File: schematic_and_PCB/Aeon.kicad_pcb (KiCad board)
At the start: 2 copper layers, 70 x 52 mm, 137 parts, among them IC1 AEM10941-QFN, IC2 STM32L412K8T6, IC3 FM25L04B-GTR, IC4 TPS7A0233PDBVR, J1 Conn_01x06_Pin, J2 FH34SRJ-50S-0.5SH50 - Colour 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, J3 Micro_SD_Card, Q1 BSS138, Q2 SI2301CDS-T1-E3, Q4 SI2301CDS-T1-E3, Q5 BSS138, SW1 SW_EHV_EN, SW2 REFRESH_BTN, SW3 RESET_BTN, SW4 SW_DIP_x06_SMD_1.27, SW5 SW_DIP_x06_SMD_1.27

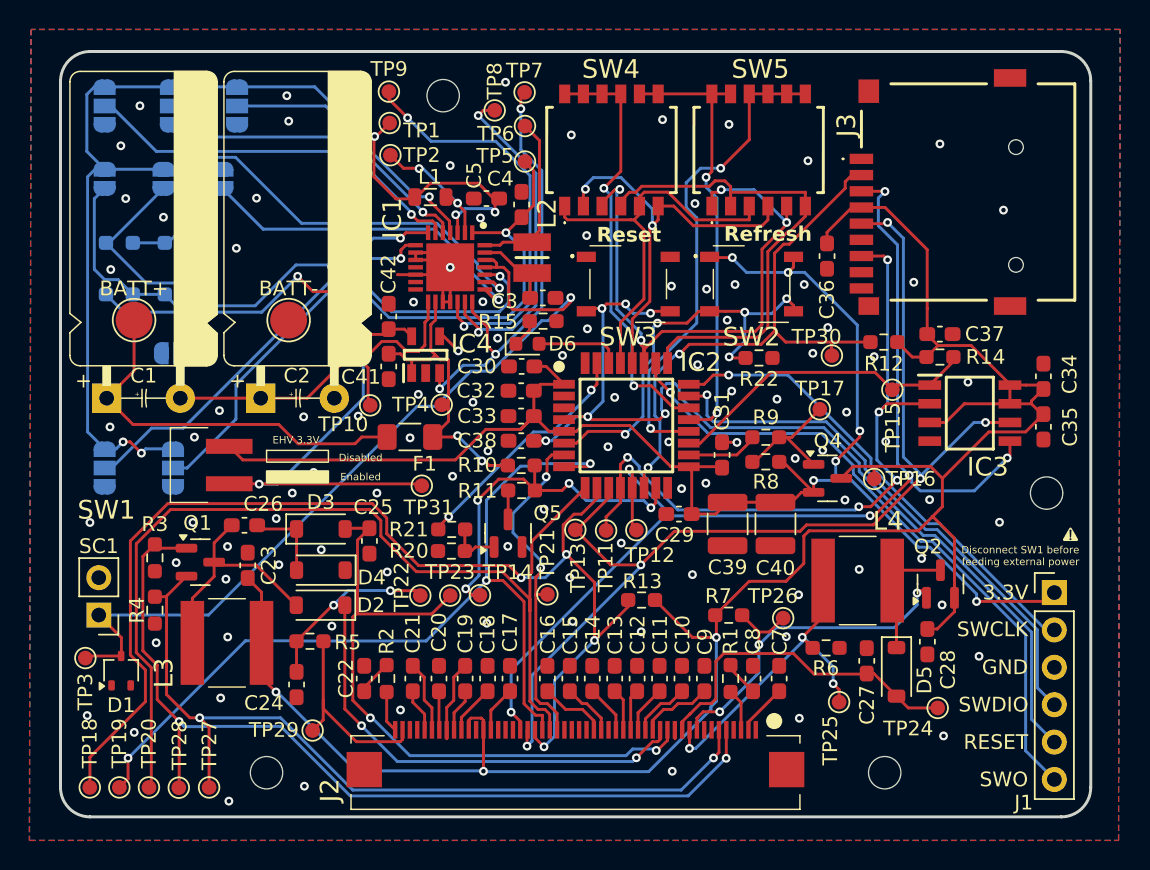
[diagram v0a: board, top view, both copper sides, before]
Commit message: Change electrical design to match Spectra 6 driver reference
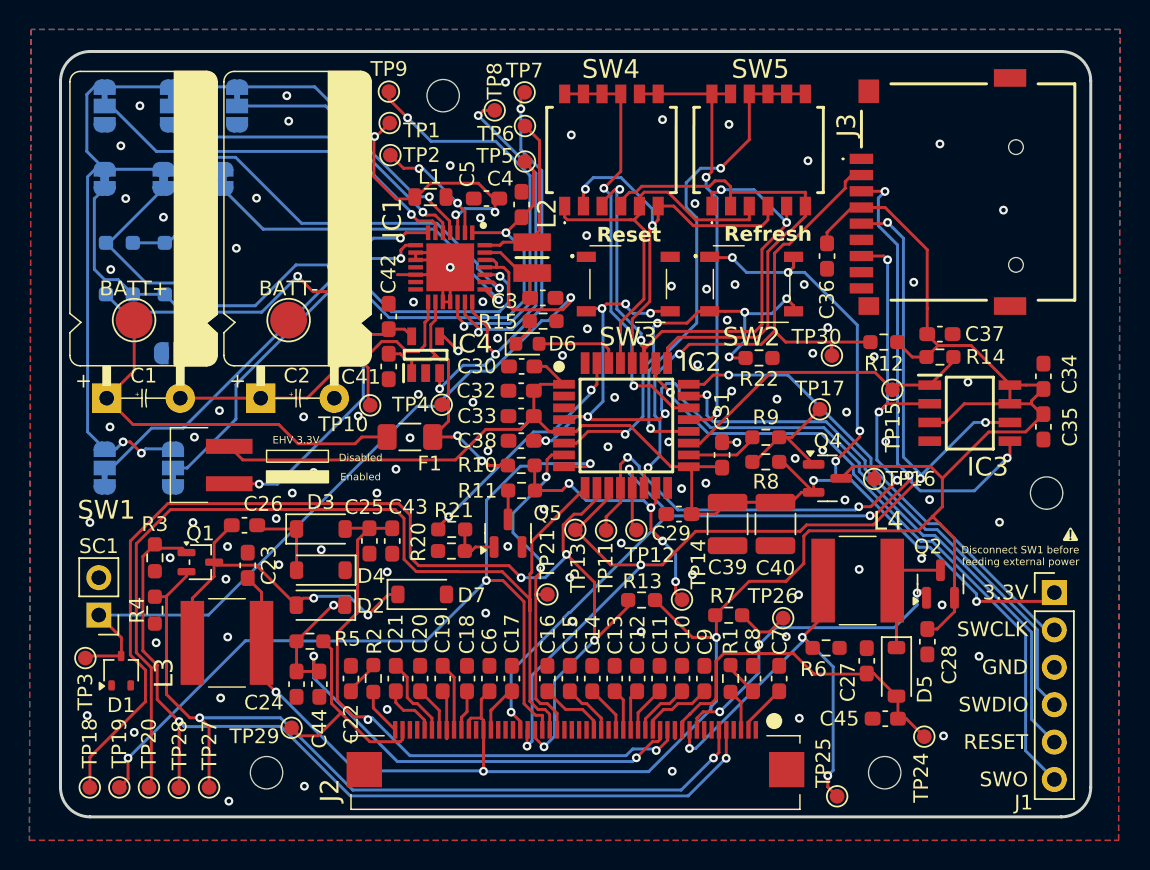
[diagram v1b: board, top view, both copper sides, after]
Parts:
- removed TP22, TP23, TP31: ~, TestPoint:TestPoint_Pad_D1.0mm
- added C43: 100nF/50V, Capacitor_SMD:C_0603_1608Metric_Pad1.08x0.95mm_HandSolder, F.Cu at (137.5, 108.3)
- added C44: 100nF/50V, Capacitor_SMD:C_0603_1608Metric_Pad1.08x0.95mm_HandSolder, F.Cu at (132.6, 118.0)
- added C45: 100nF/50V, Capacitor_SMD:C_0603_1608Metric_Pad1.08x0.95mm_HandSolder, F.Cu at (171.0, 120.3)
- added C6: 100nF/50V, Capacitor_SMD:C_0603_1608Metric_Pad1.08x0.95mm_HandSolder, F.Cu at (144.1, 117.6)
- added D7: BZT52C27, Diode_SMD:D_SOD-123, F.Cu at (139.6, 111.9)
- C15, C16: value 10uF/25V -> 1uF/50V
- C17: value 2.2uF/6V -> 2.2uF/6.3V
- C18, C19, C20, C21: value 1uF/10V -> 1uF/50V
- C23, C7: value 4.7uF/10V -> 4.7uF/25V
- JP1, JP2, JP3: footprint Jumper:SolderJumper-3_P1.3mm_Open_RoundedPad1.0x1.5mm -> Aeon:SolderJumper-3_P1.3mm_Bridged2Bar23_RoundedPad1.0x1.5mm
- JP5, JP6, JP7: footprint Jumper:SolderJumper-2_P1.3mm_Open_RoundedPad1.0x1.5mm -> Jumper:SolderJumper-2_P1.3mm_Bridged_RoundedPad1.0x1.5mm
- JP8, JP9: footprint Jumper:SolderJumper-3_P1.3mm_Open_RoundedPad1.0x1.5mm -> Aeon:SolderJumper-3_P1.3mm_Bridged2Bar12_RoundedPad1.0x1.5mm
- Q1: value BSS138 -> SI1308EDL; footprint Package_TO_SOT_SMD:SOT-23 -> Package_TO_SOT_SMD:SOT-323_SC-70
- R4, R6: value 0.47R -> 0.2R
- moved TP14 13.7 mm to (157.2, 112.2)
- moved TP25 6.40 mm to (167.8, 125.6)
- moved TP24 2.15 mm to (173.7, 121.5)
- moved C19 1.52 mm to (141.0, 117.6), turned to -90 degrees
- moved TP29 1.44 mm to (130.7, 121.0)
- moved C18 1.40 mm to (142.6, 117.6)
- moved C20 1.28 mm to (139.4, 117.6)
- moved C21 1.16 mm to (137.8, 117.6)
- moved C22 0.90 mm to (134.7, 117.6)
- moved R2 0.90 mm to (136.3, 117.6)
- moved C17 0.13 mm to (145.7, 117.6)
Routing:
- net Net-(IC4-OUT): track 30.6 -> 19.5 mm
- net Net-(D2-A): track 15.9 -> 24.2 mm, vias 0 -> 2
- net DISP_RESEC: track 23.2 -> 29.8 mm
- net DISP_VPH: track 44.1 -> 38.3 mm, vias 4 -> 3
- net Net-(IC2-PB1): track 24.7 -> 19.3 mm
- net DISP_VGL: track 45.3 -> 41.6 mm
- net +3.3V AUX: track 146.4 -> 148.6 mm
- net Net-(J2-CP2P): track 5.56 -> 3.65 mm
- net Net-(J2-CP2N): track 2.94 -> 4.68 mm
- net DISP_VGH: track 14.0 -> 15.3 mm
- net DISP_CS: track 79.1 -> 80.1 mm
- net DISP_BUSY: track 67.5 -> 68.5 mm
- net Net-(J2-CP1P): track 2.96 -> 3.88 mm
- net DISP_VPC: track 22.9 -> 23.7 mm
- net Net-(J2-VCP2): track 3.36 -> 2.66 mm
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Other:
- board text added: "v2.0"
- board text removed: "v1.4"
